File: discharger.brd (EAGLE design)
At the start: 35.6 x 69.8 mm, 109 parts, among them U1 BW6101, U10 BW6101, U11 BW6101, U12 BW6101, U2 BW6101, U3 BW6101, U4 BW6101, U5 BW6101, U6 BW6101, U7 BW6101, U8 BW6101, U9 BW6101

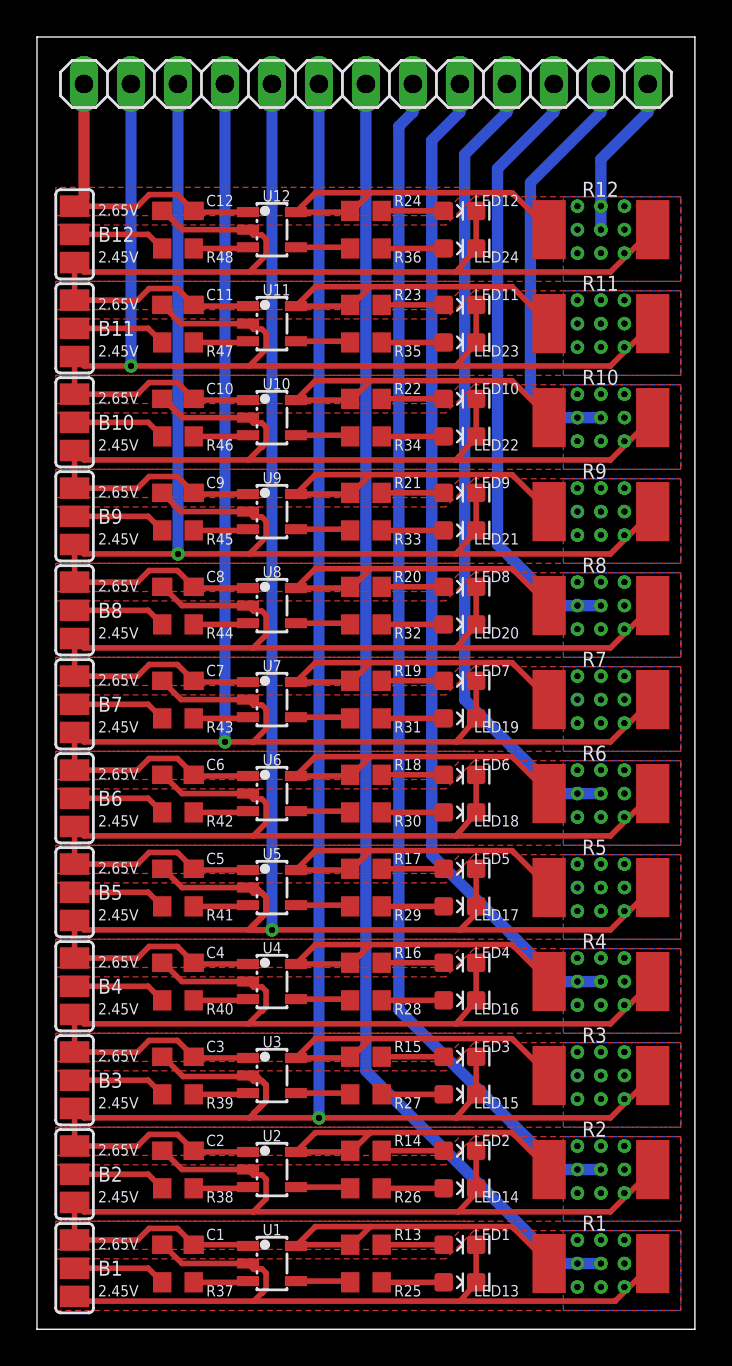
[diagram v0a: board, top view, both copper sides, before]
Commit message: adjust labels, add traces to pre-set 2.45V
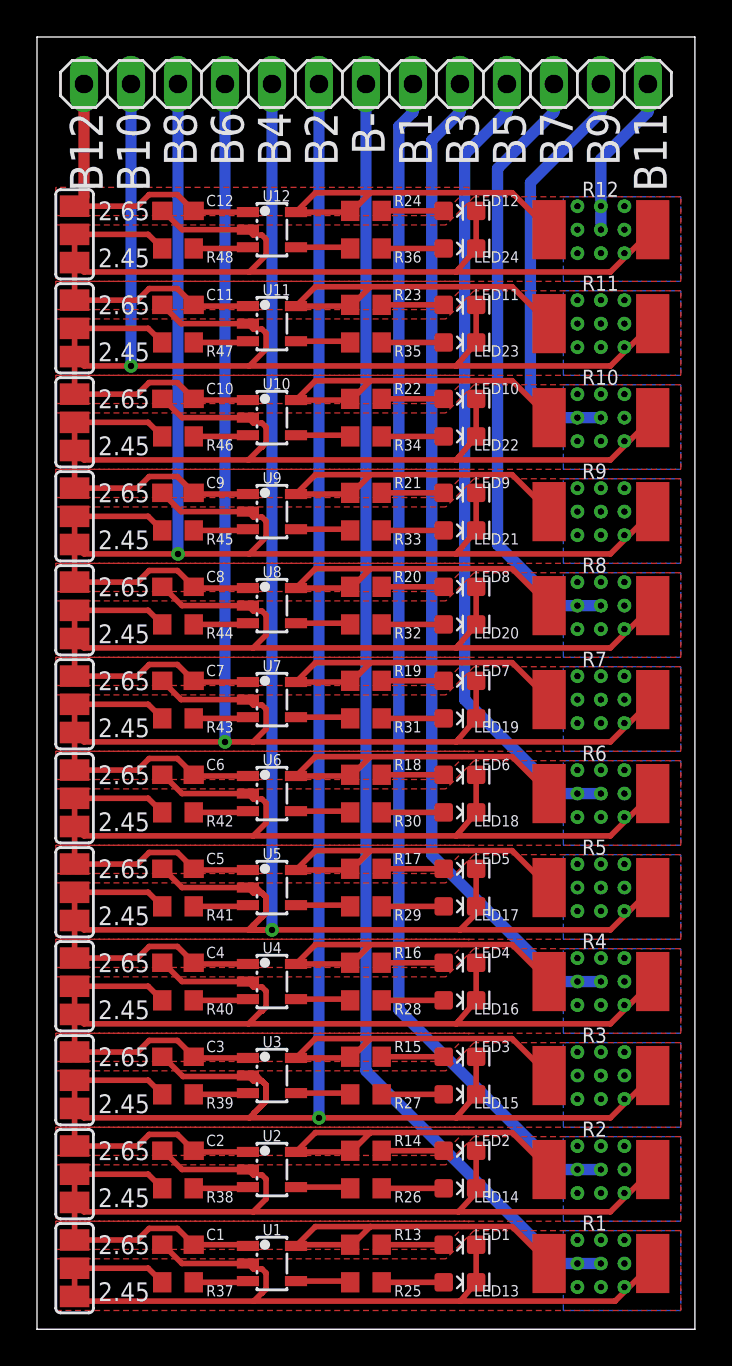
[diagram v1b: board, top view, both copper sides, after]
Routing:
- net N$78: track 0.00 -> 1.52 mm
- net N$77: track 0.00 -> 1.52 mm
- net N$76: track 0.00 -> 1.52 mm
- net N$72: track 0.00 -> 1.52 mm
- net N$70: track 0.00 -> 1.52 mm
- net N$69: track 0.00 -> 1.52 mm
- net N$67: track 0.00 -> 1.52 mm
- net N$82: track 0.00 -> 1.52 mm
- net N$80: track 0.00 -> 1.52 mm
- net N$79: track 0.00 -> 1.52 mm
- net N$73: track 0.00 -> 1.52 mm
- net N$68: track 0.00 -> 1.52 mm
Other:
- board text added: "2.45"
- board text added: "2.65"
- board text removed: "2.45V"
- board text removed: "2.65V"
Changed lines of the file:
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@@
 <wire x1="35.56" y1="69.85" x2="0" y2="69.85" width="0" layer="20"/>
 <wire x1="0" y1="69.85" x2="0" y2="0" width="0" layer="20"/>
-<text x="3.302" y="1.778" size="0.6096" layer="25">2.45V</text>
-<text x="3.302" y="4.318" size="0.6096" layer="25">2.65V</text>
-<text x="3.302" y="6.858" size="0.6096" layer="25">2.45V</text>
-<text x="3.302" y="9.398" size="0.6096" layer="25">2.65V</text>
-<text x="3.302" y="11.938" size="0.6096" layer="25">2.45V</text>
-<text x="3.302" y="14.478" size="0.6096" layer="25">2.65V</text>
-<text x="3.302" y="17.018" size="0.6096" layer="25">2.45V</text>
-<text x="3.302" y="19.558" size="0.6096" layer="25">2.65V</text>
-<text x="3.302" y="22.098" size="0.6096" layer="25">2.45V</text>
-<text x="3.302" y="24.638" size="0.6096" layer="25">2.65V</text>
-<text x="3.302" y="27.178" size="0.6096" layer="25">2.45V</text>
-<text x="3.302" y="29.718" size="0.6096" layer="25">2.65V</text>
-<text x="3.302" y="32.258" size="0.6096" layer="25">2.45V</text>
-<text x="3.302" y="34.798" size="0.6096" layer="25">2.65V</text>
-<text x="3.302" y="37.338" size="0.6096" layer="25">2.45V</text>
-<text x="3.302" y="39.878" size="0.6096" layer="25">2.65V</text>
-<text x="3.302" y="42.418" size="0.6096" layer="25">2.45V</text>
-<text x="3.302" y="44.958" size="0.6096" layer="25">2.65V</text>
-<text x="3.302" y="47.498" size="0.6096" layer="25">2.45V</text>
-<text x="3.302" y="50.038" size="0.6096" layer="25">2.65V</text>
-<text x="3.302" y="52.578" size="0.6096" layer="25">2.45V</text>
-<text x="3.302" y="55.118" size="0.6096" layer="25">2.65V</text>
-<text x="3.302" y="57.658" size="0.6096" layer="25">2.45V</text>
-<text x="3.302" y="60.198" size="0.6096" layer="25">2.65V</text>
+<text x="3.302" y="2.032" size="1.016" layer="25" align="center-left">2.45</text>
+<text x="3.302" y="4.572" size="1.016" layer="25" align="center-left">2.65</text>
+<text x="3.302" y="7.112" size="1.016" layer="25" align="center-left">2.45</text>
+<text x="3.302" y="9.652" size="1.016" layer="25" align="center-left">2.65</text>
+<text x="3.302" y="12.192" size="1.016" layer="25" align="center-left">2.45</text>
+<text x="3.302" y="14.732" size="1.016" layer="25" align="center-left">2.65</text>
+<text x="3.302" y="17.272" size="1.016" layer="25" align="center-left">2.45</text>
+<text x="3.302" y="19.812" size="1.016" layer="25" align="center-left">2.65</text>
+<text x="3.302" y="22.352" size="1.016" layer="25" align="center-left">2.45</text>
+<text x="3.302" y="24.892" size="1.016" layer="25" align="center-left">2.65</text>
+<text x="3.302" y="27.432" size="1.016" layer="25" align="center-left">2.45</text>
+<text x="3.302" y="29.972" size="1.016" layer="25" align="center-left">2.65</text>
+<text x="3.302" y="32.512" size="1.016" layer="25" align="center-left">2.45</text>
+<text x="3.302" y="35.052" size="1.016" layer="25" align="center-left">2.65</text>
+<text x="3.302" y="37.592" size="1.016" layer="25" align="center-left">2.45</text>
+<text x="3.302" y="40.132" size="1.016" layer="25" align="center-left">2.65</text>
+<text x="3.302" y="42.672" size="1.016" layer="25" align="center-left">2.45</text>
+<text x="3.302" y="45.212" size="1.016" layer="25" align="center-left">2.65</text>
+<text x="3.302" y="47.752" size="1.016" layer="25" align="center-left">2.45</text>
+<text x="3.302" y="50.292" size="1.016" layer="25" align="center-left">2.65</text>
+<text x="3.302" y="52.832" size="1.016" layer="25" align="center-left">2.45</text>
+<text x="3.302" y="55.372" size="1.016" layer="25" align="center-left">2.65</text>
+<text x="3.302" y="57.912" size="1.016" layer="25" align="center-left">2.45</text>
+<text x="3.302" y="60.452" size="1.016" layer="25" align="center-left">2.65</text>
 <text x="1.27" y="1.27" size="1.778" layer="26" rot="MR90">https://tinyurl.com/LTOBalance</text>
 <text x="25.4" y="27.94" size="1.778" layer="26" rot="MR90">&gt;REV</text>
 <text x="25.4" y="1.27" size="1.778" layer="26" rot="MR90">BW6101 Discharger</text>
 <text x="3.556" y="60.198" size="1.778" layer="26" rot="MR270" align="bottom-right">B12</text>
-<text x="6.096" y="60.452" size="1.778" layer="26" rot="MR270" align="bottom-right">B10</text>
+<text x="6.096" y="60.198" size="1.778" layer="26" rot="MR270" align="bottom-right">B10</text>
 <text x="8.636" y="60.198" size="1.778" layer="26" rot="MR270" align="bottom-right">B8</text>
 <text x="11.176" y="60.198" size="1.778" layer="26" rot="MR270" align="bottom-right">B6</text>
@@
 <text x="31.496" y="60.198" size="1.778" layer="26" rot="MR270" align="bottom-right">B9</text>
 <text x="34.036" y="60.198" size="1.778" layer="26" rot="MR270" align="bottom-right">B11</text>
-<text x="3.302" y="3.302" size="0.8128" layer="25" align="center-left">B1</text>
-<text x="3.302" y="8.382" size="0.8128" layer="25" align="center-left">B2</text>
-<text x="3.302" y="13.462" size="0.8128" layer="25" align="center-left">B3</text>
-<text x="3.302" y="18.542" size="0.8128" layer="25" align="center-left">B4</text>
-<text x="3.302" y="23.622" size="0.8128" layer="25" align="center-left">B5</text>
-<text x="3.302" y="28.702" size="0.8128" layer="25" align="center-left">B6</text>
-<text x="3.302" y="33.782" size="0.8128" layer="25" align="center-left">B7</text>
-<text x="3.302" y="38.862" size="0.8128" layer="25" align="center-left">B8</text>
-<text x="3.302" y="43.942" size="0.8128" layer="25" align="center-left">B9</text>
-<text x="3.302" y="49.022" size="0.8128" layer="25" align="center-left">B10</text>
-<text x="3.302" y="54.102" size="0.8128" layer="25" align="center-left">B11</text>
-<text x="3.302" y="59.182" size="0.8128" layer="25" align="center-left">B12</text>
+<text x="3.556" y="65.786" size="1.778" layer="25" rot="R90" align="bottom-right">B12</text>
+<text x="6.096" y="65.786" size="1.778" layer="25" rot="R90" align="bottom-right">B10</text>
+<text x="8.636" y="65.786" size="1.778" layer="25" rot="R90" align="bottom-right">B8</text>
+<text x="11.176" y="65.786" size="1.778" layer="25" rot="R90" align="bottom-right">B6</text>
+<text x="13.716" y="65.786" size="1.778" layer="25" rot="R90" align="bottom-right">B4</text>
+<text x="16.256" y="65.786" size="1.778" layer="25" rot="R90" align="bottom-right">B2</text>
+<text x="18.796" y="65.786" size="1.778" layer="25" rot="R90" align="bottom-right">B-</text>
+<text x="21.336" y="65.786" size="1.778" layer="25" rot="R90" align="bottom-right">B1</text>
+<text x="23.876" y="65.786" size="1.778" layer="25" rot="R90" align="bottom-right">B3</text>
+<text x="26.416" y="65.786" size="1.778" layer="25" rot="R90" align="bottom-right">B5</text>
+<text x="28.956" y="65.786" size="1.778" layer="25" rot="R90" align="bottom-right">B7</text>
+<text x="31.496" y="65.786" size="1.778" layer="25" rot="R90" align="bottom-right">B9</text>
+<text x="34.036" y="65.786" size="1.778" layer="25" rot="R90" align="bottom-right">B11</text>
 </plain>
 <attributes>
@@
 <wire x1="11.4" y1="23.876" x2="11.694" y2="23.582" width="0.3048" layer="1"/>
 <wire x1="11.43" y1="21.59" x2="12.7" y2="21.59" width="0.3048" layer="1"/>
-<wire x1="23.737" y1="22.86" x2="23.737" y2="22.625371875" width="0.3048" layer="1"/>
 <wire x1="30.994" y1="21.59" x2="33.28" y2="23.876" width="0.3048" layer="1"/>
 <contactref element="SJ4" pad="3"/>
@@
 <wire x1="10.922" y1="2.54" x2="11.4" y2="2.606" width="0.3048" layer="1"/>
 </signal>
+<signal name="N$67">
+<wire x1="2.032" y1="59.182" x2="2.032" y2="57.658" width="0.3048" layer="1"/>
+</signal>
+<signal name="N$68">
+<wire x1="2.032" y1="54.102" x2="2.032" y2="52.578" width="0.3048" layer="1"/>
+</signal>
+<signal name="N$69">
+<wire x1="2.032" y1="49.022" x2="2.032" y2="47.498" width="0.3048" layer="1"/>
+</signal>
+<signal name="N$70">
+<wire x1="2.032" y1="43.942" x2="2.032" y2="42.418" width="0.3048" layer="1"/>
+</signal>
+<signal name="N$72">
+<wire x1="2.032" y1="38.862" x2="2.032" y2="37.338" width="0.3048" layer="1"/>
+</signal>
+<signal name="N$73">
+<wire x1="2.032" y1="33.782" x2="2.032" y2="32.258" width="0.3048" layer="1"/>
+</signal>
+<signal name="N$76">
+<wire x1="2.032" y1="28.702" x2="2.032" y2="27.178" width="0.3048" layer="1"/>
+</signal>
+<signal name="N$77">
+<wire x1="2.032" y1="23.622" x2="2.032" y2="22.098" width="0.3048" layer="1"/>
+</signal>
+<signal name="N$78">
+<wire x1="2.032" y1="18.542" x2="2.032" y2="17.018" width="0.3048" layer="1"/>
+</signal>
+<signal name="N$79">
+<wire x1="2.032" y1="13.462" x2="2.032" y2="11.938" width="0.3048" layer="1"/>
+</signal>
+<signal name="N$80">
+<wire x1="2.032" y1="8.382" x2="2.032" y2="6.858" width="0.3048" layer="1"/>
+</signal>
+<signal name="N$82">
+<wire x1="2.032" y1="3.302" x2="2.032" y2="1.778" width="0.3048" layer="1"/>
+</signal>
 </signals>
